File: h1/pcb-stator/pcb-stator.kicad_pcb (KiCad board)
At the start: 2 copper layers, 92.5 x 126.1 mm, 1660 parts, among them J1 Conn_01x01_Pin

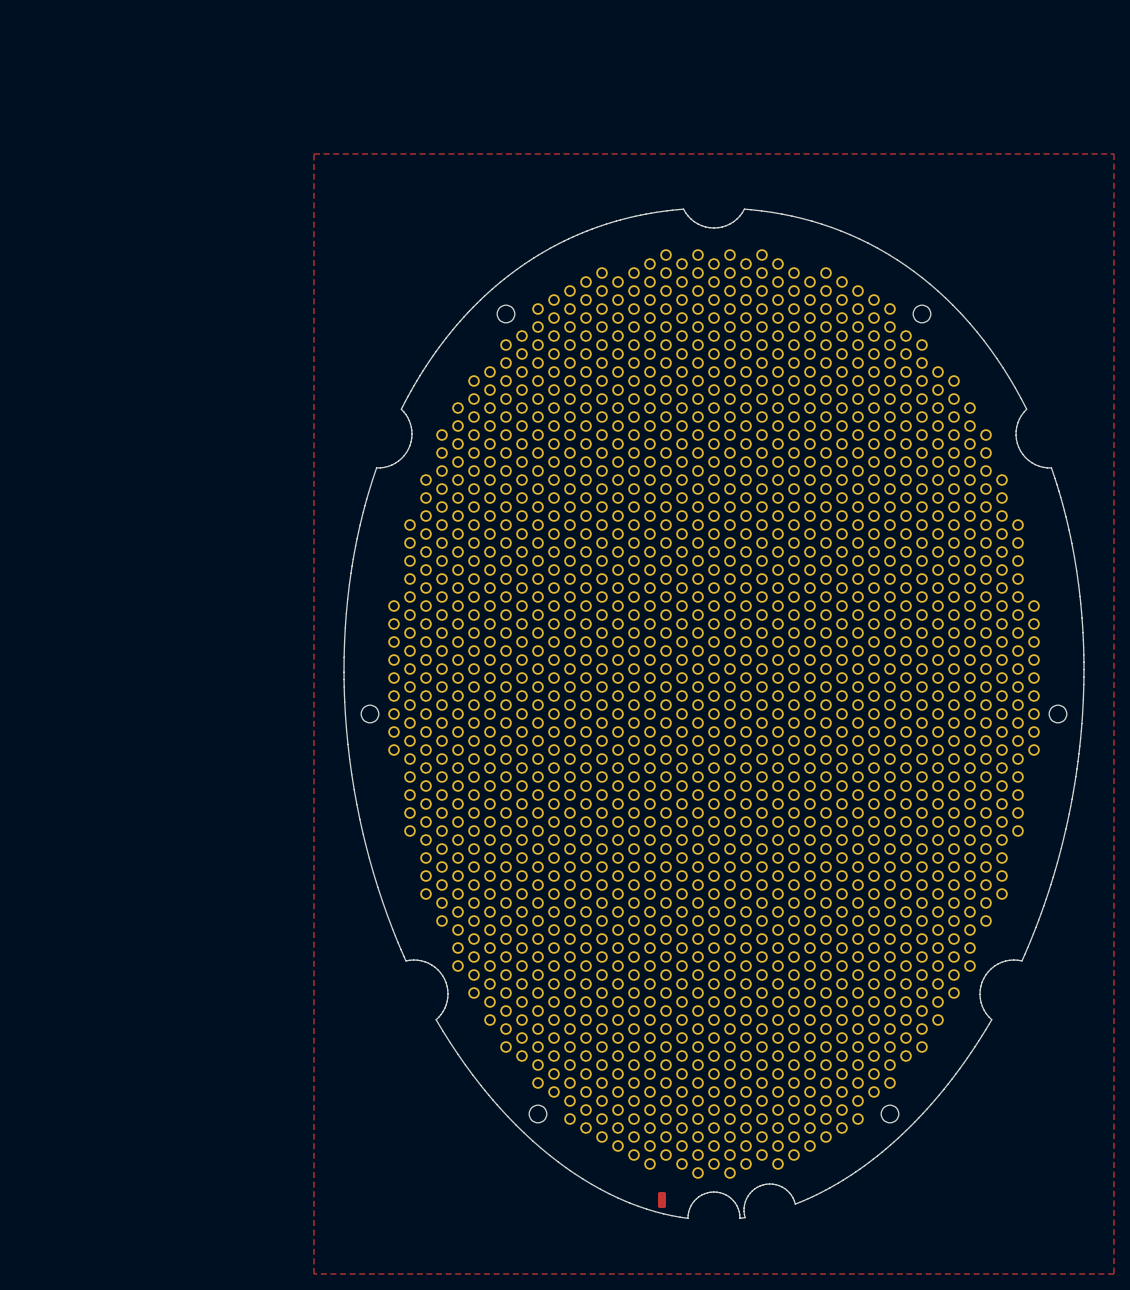
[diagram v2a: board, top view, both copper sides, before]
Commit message: h1: changed stator hole size (1.25mm) & updated images
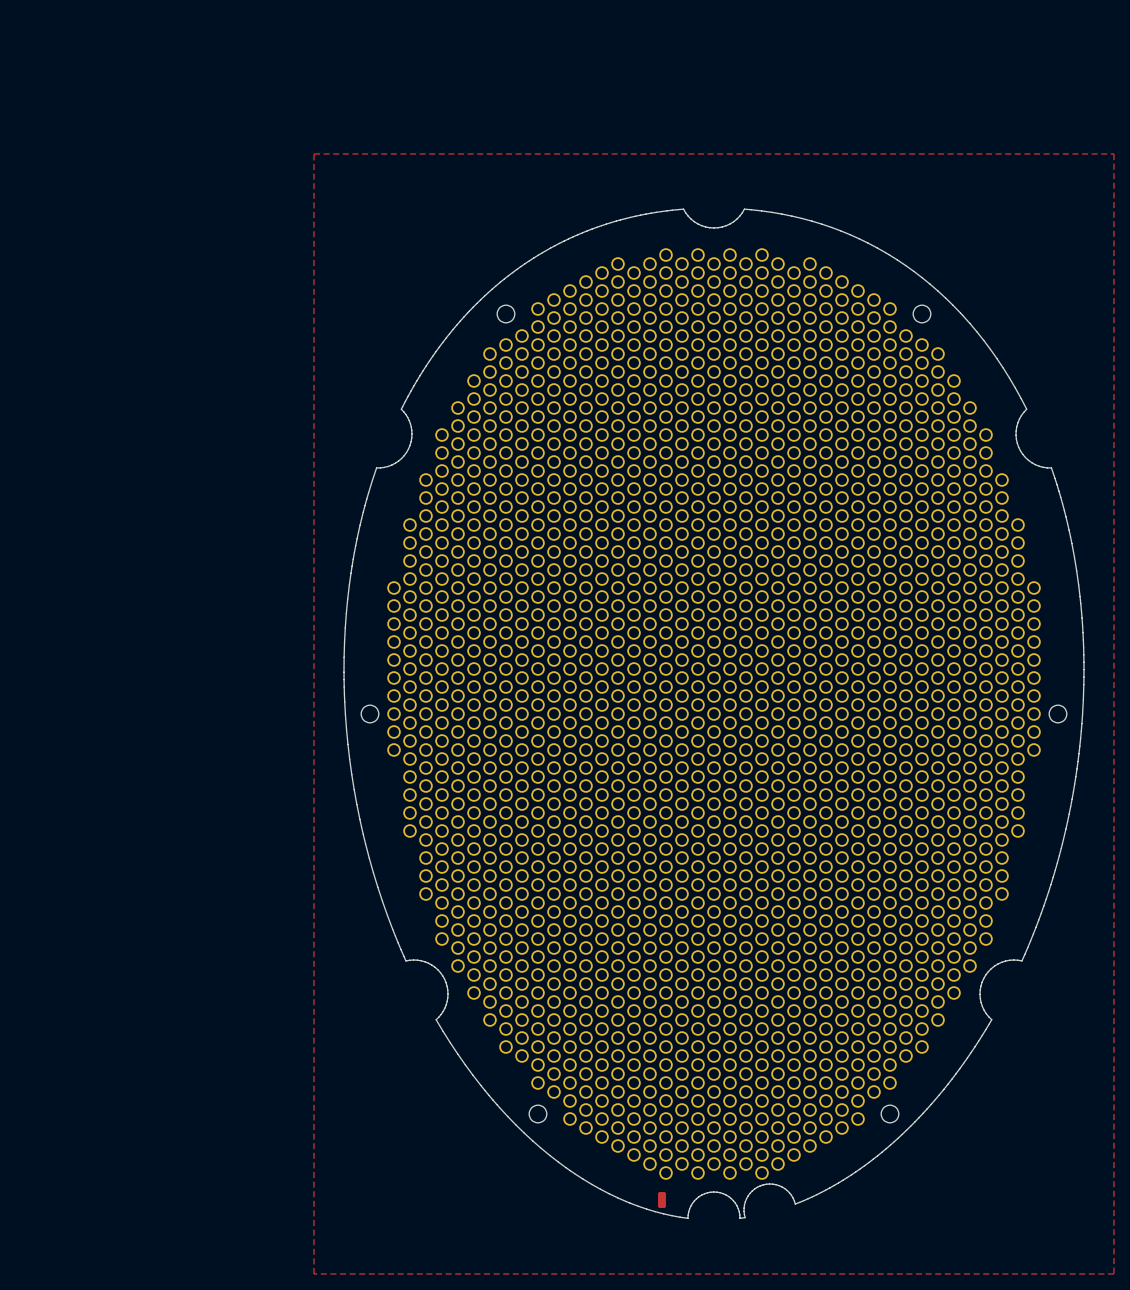
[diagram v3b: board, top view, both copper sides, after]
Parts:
- added H1: MountingHole_Pad, MountingHole:MountingHole_2.2mm_M2_DIN965_Pad, F.Cu at (140.0, 84.2)
- added H1: MountingHole_Pad, MountingHole:MountingHole_2.2mm_M2_DIN965_Pad, F.Cu at (66.0, 128.1)
- added H1: MountingHole_Pad, MountingHole:MountingHole_2.2mm_M2_DIN965_Pad, F.Cu at (134.0, 128.1)
- added H1: MountingHole_Pad, MountingHole:MountingHole_2.2mm_M2_DIN965_Pad, F.Cu at (94.0, 157.4)
- added H1: MountingHole_Pad, MountingHole:MountingHole_2.2mm_M2_DIN965_Pad, F.Cu at (128.0, 55.0)
- added H1: MountingHole_Pad, MountingHole:MountingHole_2.2mm_M2_DIN965_Pad, F.Cu at (112.0, 43.8)
- added H1: MountingHole_Pad, MountingHole:MountingHole_2.2mm_M2_DIN965_Pad, F.Cu at (106.0, 157.4)
- added H1: MountingHole_Pad, MountingHole:MountingHole_2.2mm_M2_DIN965_Pad, F.Cu at (72.0, 55.0)
- added H1: MountingHole_Pad, MountingHole:MountingHole_2.2mm_M2_DIN965_Pad, F.Cu at (60.0, 84.2)
- added H1: MountingHole_Pad, MountingHole:MountingHole_2.2mm_M2_DIN965_Pad, F.Cu at (88.0, 43.8)
